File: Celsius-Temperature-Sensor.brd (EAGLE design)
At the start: 11.9 x 23 mm, 17 parts, among them Q1 BSS138, Q2 BSS138

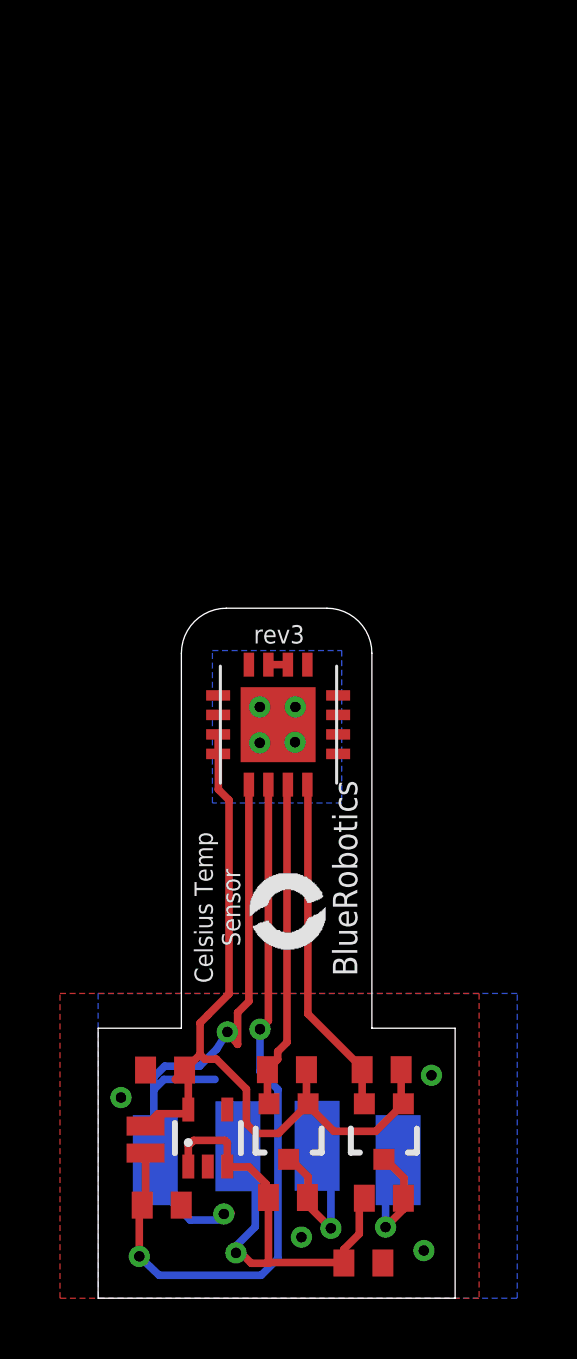
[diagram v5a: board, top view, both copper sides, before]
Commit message: Fixed for compatibility with DroneCode autopilots.
Removed logic level converters.
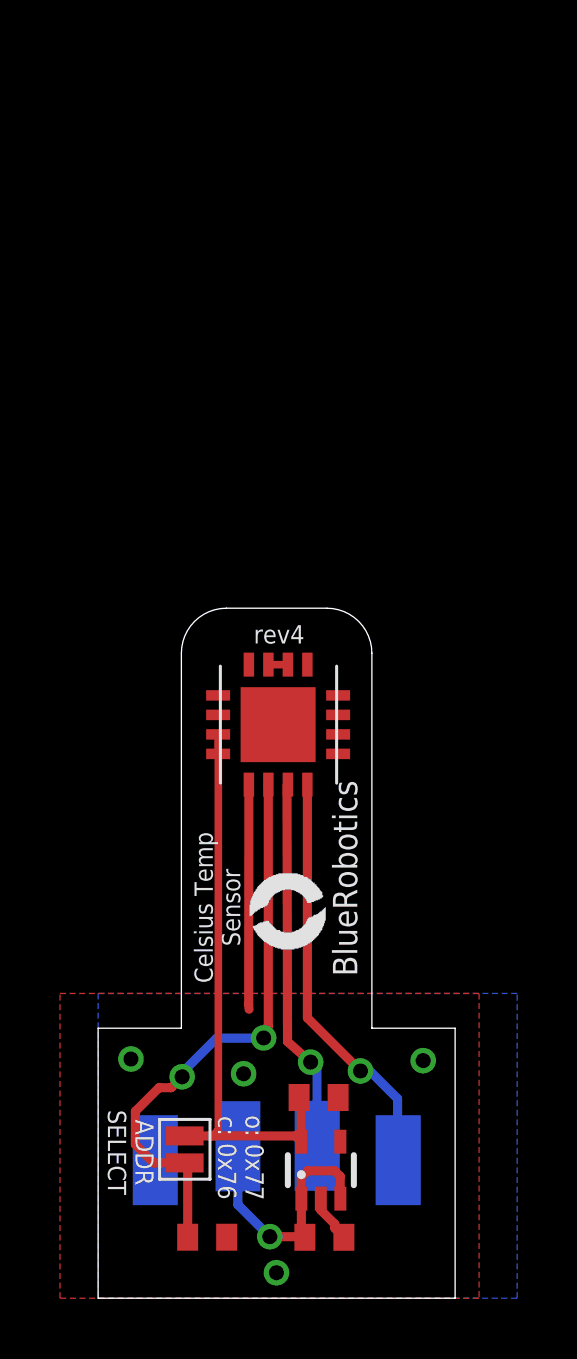
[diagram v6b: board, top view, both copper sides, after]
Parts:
- removed Q1, Q2: BSS138, SparkFun-DiscreteSemi:SOT323
- removed R2, R3, R4, R5: 10K, resistor:R0402
- moved C2 5.20 mm to (7.35, 6.69), turned to 0 degrees
- moved U$1 3.92 mm to (7.42, 4.27)
- moved R6 1.85 mm to (3.64, 2.03)
- moved C3 1.56 mm to (7.54, 2.03)
- moved SJ1 1.34 mm to (2.88, 4.96)
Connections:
- removed net SCL_HV: Q2.3, R5.1, U$5.P$1
- removed net SCL_LV: Q2.2, R4.1, U$8.3
- removed net SDA_HV: Q1.3, R3.1, U$6.P$1
- removed net SDA_LV: Q1.2, R2.1, U$8.4
- new net SCL: U$5.P$1, U$8.3
- new net SDA: U$6.P$1, U$8.4
- net 3.3V: no longer Q1.1, Q2.1, R2.2, R4.2
- net VCC: no longer R3.2, R5.2
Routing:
- net SDA: track 0.00 -> 14.0 mm, vias 0 -> 1
- net SCL: track 0.00 -> 12.5 mm, vias 0 -> 1
- net GND: track 21.5 -> 9.09 mm, vias 6 -> 4
- net SDA_LV: track 11.4 -> 0.00 mm
- net SCL_LV: track 10.9 -> 0.00 mm
- net 3.3V: track 27.6 -> 18.9 mm
- net VCC: track 17.4 -> 8.89 mm
- net SCL_HV: track 5.88 -> 0.00 mm, vias 1 -> 0
- net ADDR_SEL: track 25.0 -> 19.6 mm
- net SDA_HV: track 5.22 -> 0.00 mm, vias 1 -> 0
- net TPAD: track 3.37 -> 2.55 mm, vias 4 -> 0
- removed copper zone on layer 16, net TPAD
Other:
- board text added: "ADDR SELECT"
- board text added: "o: 0x77 c: 0x76"
- board text added: "rev4"
- board text removed: "rev3"
